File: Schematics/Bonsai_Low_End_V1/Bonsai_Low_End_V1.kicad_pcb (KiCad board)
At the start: 2 copper layers, 31.9 x 20.2 mm, 23 parts, among them J1 Bat_Connector, U1 MOUDLE-SEEEDUINO-XIAO-ESP32C3, U2 MAX30101EFD, U3 1.8V, U5 DRV2605LDGS

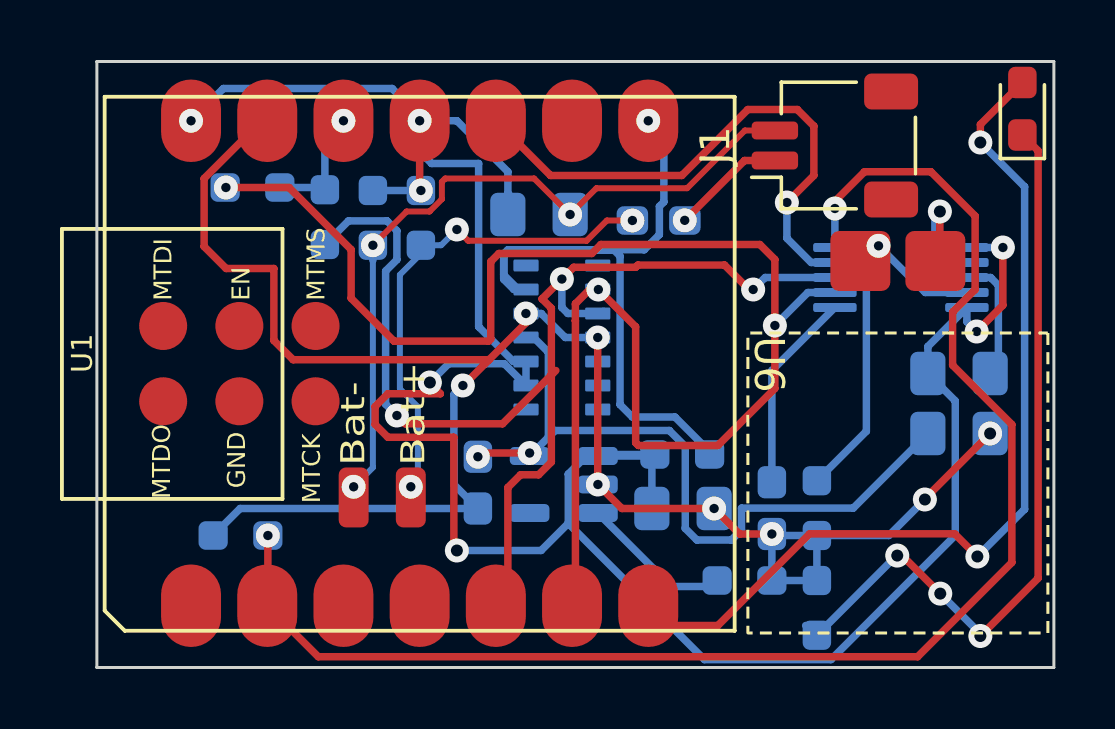
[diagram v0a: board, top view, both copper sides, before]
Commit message: Converted PCB to 4 layer
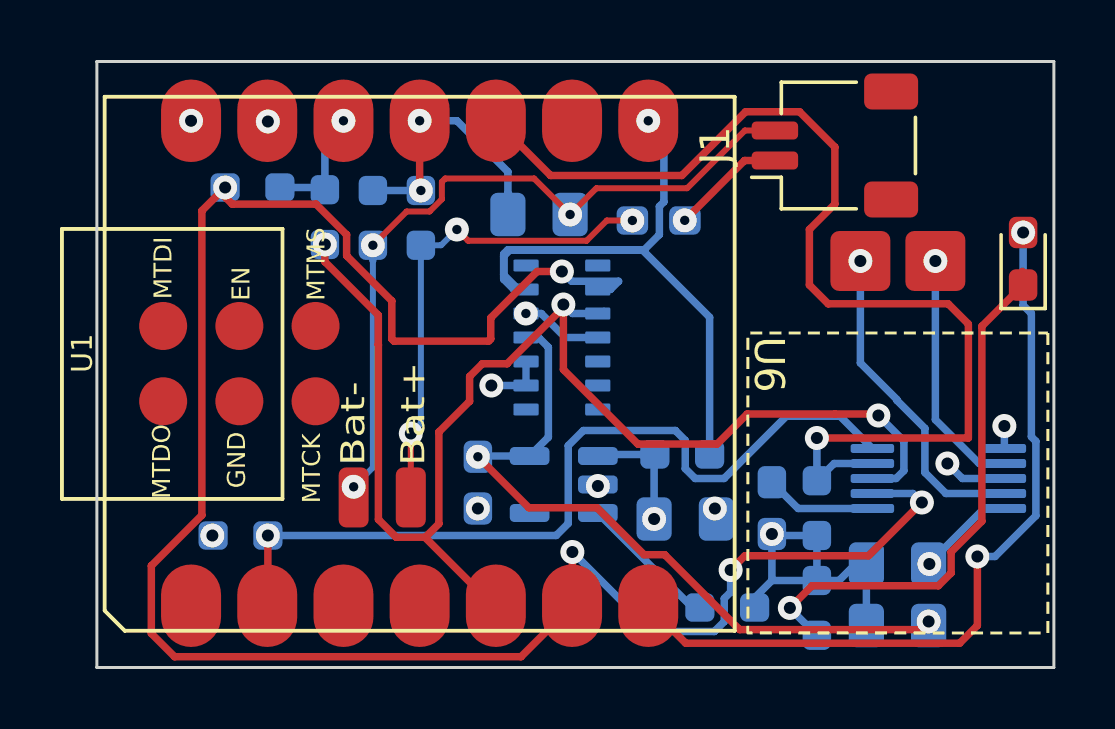
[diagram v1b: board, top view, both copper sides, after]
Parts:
- moved U5 6.82 mm to (109.3, 64.5)
- moved C4 6.72 mm to (108.0, 69.4), turned to 180 degrees
- moved C5 6.67 mm to (108.0, 67.3), turned to 180 degrees
- moved D1 5.00 mm to (112.2, 57.2)
- moved R1 1.07 mm to (102.3, 68.8)
- moved C2 0.36 mm to (100.9, 65.8)
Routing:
- net VCC: track 76.7 -> 10.1 mm
- net GND: track 66.3 -> 16.0 mm
- net HapticEN: track 49.1 -> 28.0 mm, vias 2 -> 1
- net SCL: track 53.4 -> 68.8 mm, vias 3 -> 5
- net DRV_IN/TRIG: track 27.4 -> 36.6 mm
- net Net-(D1-K): track 26.0 -> 18.2 mm, vias 3 -> 1
- net Net-(U5-OUT-): track 4.40 -> 10.9 mm
- net FUN_LIGHT: track 30.9 -> 26.7 mm
- net SDA: track 40.1 -> 44.2 mm
- net Net-(U5-OUT+): track 4.54 -> 8.35 mm
- net Net-(U5-REG): track 6.74 -> 3.76 mm
- net Bat+: track 16.9 -> 16.2 mm
- net Net-(U3-EN): track 5.27 -> 4.70 mm
- added copper zone on In1.Cu, net GND
- added copper zone on In2.Cu, net VCC
- removed copper zone on B.Cu, net GND
- removed copper zone on F.Cu, net GND
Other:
- copper layers 2 -> 4
- board text added: "BONSAI V2 Kasper Johansson William Broman Nils Kiefer"

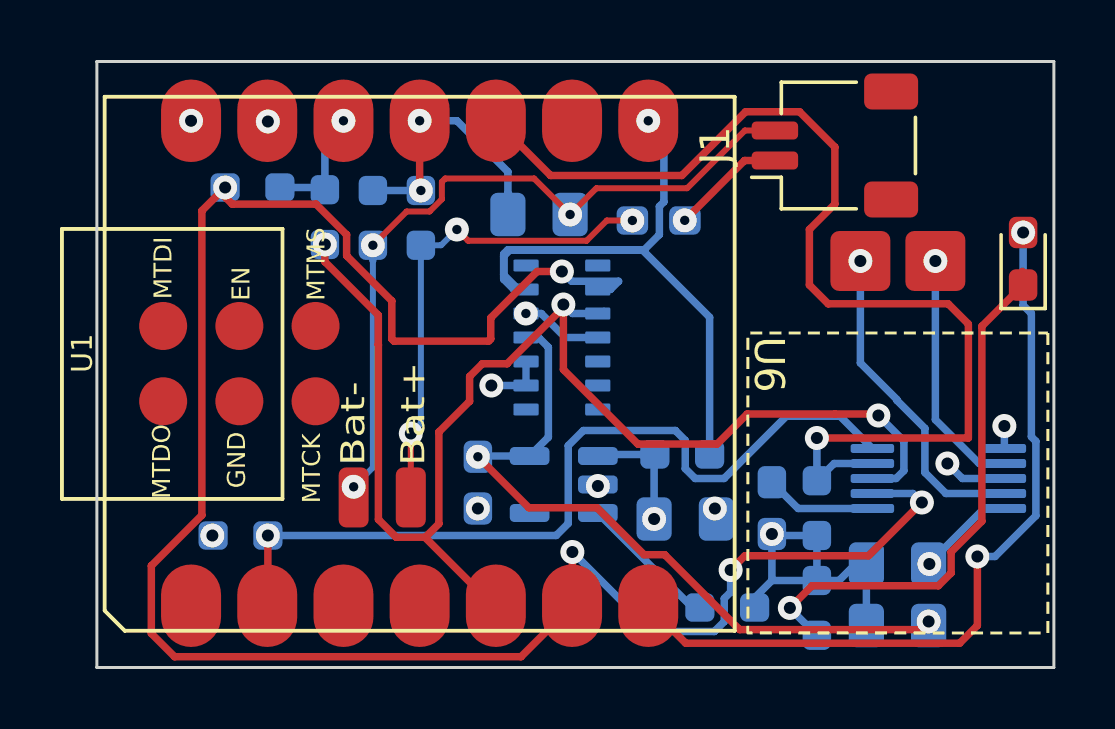
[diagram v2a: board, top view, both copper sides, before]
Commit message: Added SilkScreen References
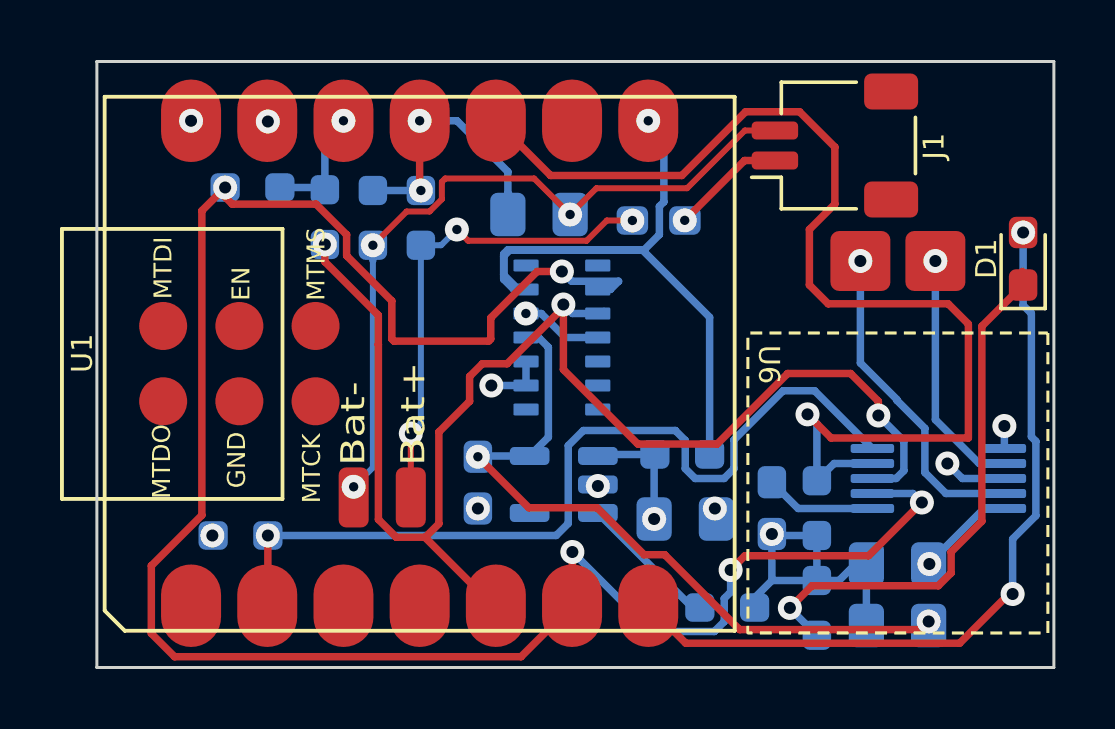
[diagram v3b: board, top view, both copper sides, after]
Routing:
- net DRV_IN/TRIG: track 36.6 -> 38.1 mm
- net SDA: track 44.2 -> 45.6 mm
- net HapticEN: track 28.0 -> 29.3 mm
